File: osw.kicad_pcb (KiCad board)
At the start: 4 copper layers, 45.6 x 41.4 mm, 59 parts, among them J1 Conn_01x02, J2 microSD_MEM2067-02-180-00-A_R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, J3 2169890001, Q1 Q_NMOS_ToshibaSMD, SW1 SPST_EVQ-P7J01P, SW2 SPST_EVQ-P7J01P, SW3 SPST_EVQ-P7J01P, SW4 SPST_EVQ-P7J01P, U1 L96-M33, U10 BMA400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

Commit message: working on the layout.
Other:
- rule pad_to_mask_clearance: 0.051 -> 0
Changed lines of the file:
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@@
   (title_block
     (title "Open-Smartwatch-GPS")
-    (date "2022-12-16")
+    (date "2023-10-21")
     (rev "${REVISION}")
   )
   (layers
-    (0 "F.Cu" power)
+    (0 "F.Cu" signal)
     (1 "In1.Cu" signal)
     (2 "In2.Cu" signal)
@@
       (dielectric_constraints no)
     )
-    (pad_to_mask_clearance 0.051)
+    (pad_to_mask_clearance 0)
+    (aux_axis_origin 160 130.6)
+    (grid_origin 160 130.6)
     (pcbplotparams
       (layerselection 0x00010fc_ffffffff)
@@
   (gr_line (start 182.6 93.8) (end 182.6 124.5)
     (stroke (width 0.05) (type solid)) (layer "Edge.Cuts"))
-  (dimension (type orthogonal) (layer "F.Cu")
-    (pts (xy 164.975 89.625) (xy 175 89.2))
-    (height -4.425)
-    (orientation 0)
-    (gr_text "10.0250 mm" (at 169.9875 83.4) (layer "F.Cu")
-      (effects (font (size 1.5 1.5) (thickness 0.3)))
-    )
-    (format (prefix "") (suffix "") (units 3) (units_format 1) (precision 4))
-    (style (thickness 0.2) (arrow_length 1.27) (text_position_mode 0) (extension_height 0.58642) (extension_offset 0.5) keep_text_aligned)
-  )
-  (dimension (type orthogonal) (layer "F.Cu")
-    (pts (xy 155.225 89.625) (xy 145.2 89.8))
-    (height -4.425)
-    (orientation 0)
-    (gr_text "10.0250 mm" (at 150.2125 83.4) (layer "F.Cu")
-      (effects (font (size 1.5 1.5) (thickness 0.3)))
-    )
-    (format (prefix "") (suffix "") (units 3) (units_format 1) (precision 4))
-    (style (thickness 0.2) (arrow_length 1.27) (text_position_mode 0) (extension_height 0.58642) (extension_offset 0.5) keep_text_aligned)
-  )
   (zone (net 1) (net_name "GND") (layer "B.Cu") (hatch edge 0.508)
     (connect_pads (clearance 0.127))

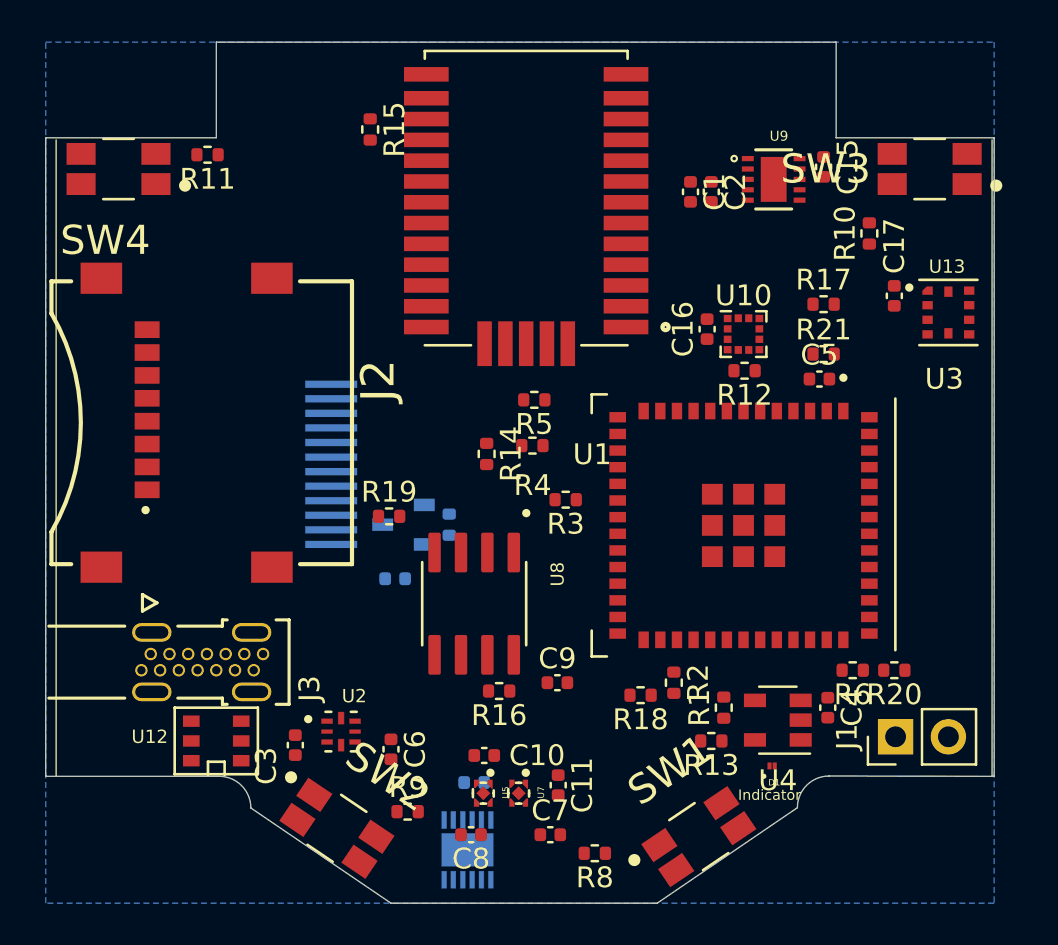
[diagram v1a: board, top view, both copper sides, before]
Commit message: Added some dimensions to the layout and corrected all the edge cuts so the board is symetric.
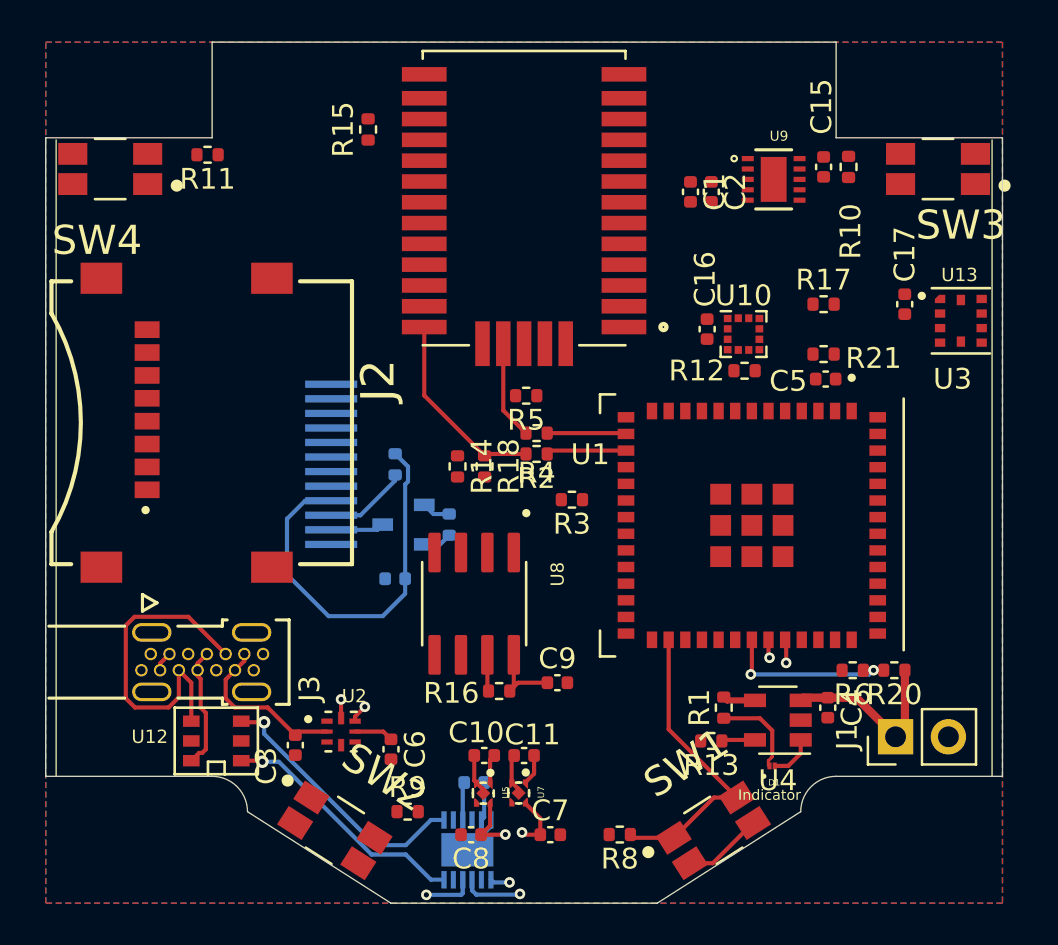
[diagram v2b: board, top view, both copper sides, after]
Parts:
- R19: moved to B.Cu
- moved R18 13.3 mm to (158.1, 109.6), turned to -90 degrees
- moved R2 12.8 mm to (160.6, 109.0), turned to 180 degrees
- moved R10 3.35 mm to (175.6, 95.2), turned to -90 degrees
- moved R19 2.52 mm to (153.8, 109.5), turned to -90 degrees
- moved C11 2.17 mm to (160.0, 123.5), turned to 180 degrees
- moved R14 1.52 mm to (156.8, 109.6)
- moved R8 1.50 mm to (164.6, 127.3)
- moved SW1 0.76 mm to (169.1, 127.1), turned to 32.52 degrees
- moved U13 0.72 mm to (181.0, 102.6)
- moved C17 0.64 mm to (178.3, 101.8)
- moved R4 0.63 mm to (160.6, 108.0)
- moved R5 0.44 mm to (160.1, 106.2)
- moved SW3 0.40 mm to (179.9, 95.3)
- moved SW4 0.40 mm to (140.1, 95.3)
- moved U3 0.40 mm to (170.9, 112.4)
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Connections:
- D1 pad 2: Net-(D1-A) -> /STAT_PWR
- R1 pad 1: Net-(D1-A) -> /STAT_PWR
- U3 pad 11: /SCL -> /TFT_CS
- U3 pad 12: /~{TFT_RST} -> /SCL
- U3 pad 13: /STAT_PWR -> /SDA
- U3 pad 14: unconnected-(U3-IO26-Pad14) -> /~{TFT_RST}
- U3 pad 15: /SDA -> /GPS_FON3V3
- U3 pad 16: /VLoad_EN -> /GPS_RX3V3
- U3 pad 21: /FLASH -> /RAM_HOLD
- U3 pad 23: GND -> unconnected-(U3-NC-Pad23)
- U3 pad 24: GND -> unconnected-(U3-NC-Pad24)
- U3 pad 28: GND -> unconnected-(U3-NC-Pad28)
- U3 pad 29: /TFT_CS -> /BTN2
- U3 pad 30: /GPS_RX3V3 -> /VLoad_EN
- U3 pad 31: /RAM_HOLD -> /STAT_PWR
- U3 pad 34: /BTN2 -> /B_MON
- U3 pad 37: GND -> unconnected-(U3-NC-Pad37)
- U3 pad 4: /B_MON -> unconnected-(U3-I36-Pad4)
- U3 pad 5: /3DFIX_3V3 -> /GEO_F3V3
- U3 pad 6: /GPS_FON3V3 -> /FLASH
- U3 pad 7: /GEO_F3V3 -> /3DFIX_3V3
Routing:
- net /TX: track 0.00 -> 26.2 mm, vias 0 -> 2
- net /3V3_2: track 0.00 -> 20.6 mm
- net /RX: track 0.00 -> 19.2 mm, vias 0 -> 2
- net /D_ESD-: track 0.00 -> 16.1 mm
- net /BTN2: track 0.00 -> 14.9 mm
- net /VCC: track 0.00 -> 14.3 mm, vias 0 -> 2
- net /VCC_SW: track 0.00 -> 13.7 mm, vias 0 -> 2
- net /D-: track 0.00 -> 13.0 mm, vias 0 -> 1
- net /D+: track 0.00 -> 12.1 mm, vias 0 -> 1
- net GND: track 0.00 -> 10.8 mm
- net /VBUS: track 0.00 -> 10.7 mm
- net /GPS_RX2V8: track 0.00 -> 9.42 mm
- net +3V3: track 0.00 -> 9.02 mm
- net /VBAT: track 0.00 -> 8.78 mm
- net /B_MON: track 0.00 -> 8.65 mm, vias 0 -> 2
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- added copper zone on F.Cu, net GND
- added copper zone on In1.Cu, net GND
- added copper zone on In2.Cu, net GND
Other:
- board size 45.6 x 41.4 mm -> 46 x 41.4 mm

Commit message: Updates to several footprints as they were not quite correct.  Finished layout.  All done on a simple two layer board.  Need to look over the design once more before ordering prototypes.
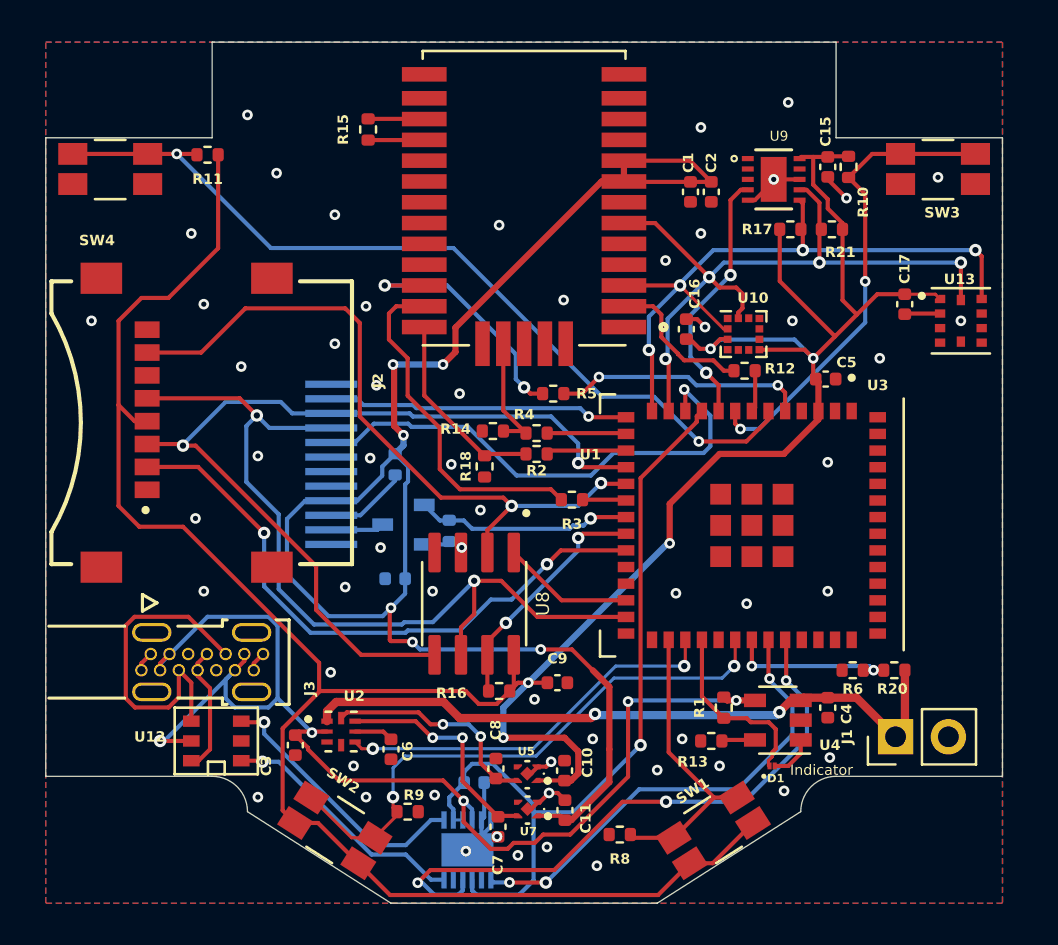
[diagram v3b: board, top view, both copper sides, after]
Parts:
- moved R21 6.01 mm to (174.8, 98.2), turned to 180 degrees
- moved R17 3.94 mm to (172.8, 98.2)
- moved C10 3.93 mm to (161.9, 124.2), turned to 90 degrees
- moved C8 3.40 mm to (158.6, 124.1), turned to 90 degrees
- moved C11 3.28 mm to (162.0, 126.1), turned to 90 degrees
- moved C7 2.54 mm to (158.7, 126.9), turned to -90 degrees
- moved R14 2.40 mm to (158.5, 107.9), turned to 180 degrees
- moved U5 2.31 mm to (160.2, 124.4), turned to 180 degrees
- moved R5 1.30 mm to (161.4, 106.1)
- moved C16 1.00 mm to (167.8, 103.0)
- moved U7 0.88 mm to (160.2, 126.1), turned to 180 degrees
- moved R7 0.30 mm to (156.4, 112.7)
- moved C15 0.20 mm to (174.6, 95.2)
- turned SW2 to -32.519 degrees
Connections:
- C16 pad 2: Net-(U10-GND) -> GND
- U10 pad 1: Net-(U10-GND) -> GND
- U10 pad 8: Net-(U10-GND) -> GND
- U10 pad 9: Net-(U10-GND) -> GND
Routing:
- net +3V3: track 9.02 -> 149.8 mm, vias 0 -> 5
- net /3V3_2: track 20.6 -> 75.3 mm, vias 0 -> 6
- net /VBUS: track 10.7 -> 59.2 mm, vias 0 -> 5
- net /MOSI: track 0.00 -> 43.3 mm, vias 0 -> 2
- net /SCLK: track 0.00 -> 41.5 mm, vias 0 -> 2
- net /FLASH: track 0.00 -> 41.0 mm, vias 0 -> 2
- net /SCL: track 0.00 -> 34.0 mm, vias 0 -> 4
- net /v3p3USB: track 4.74 -> 38.7 mm
- net /MISO: track 0.00 -> 33.7 mm, vias 0 -> 2
- net /SDA: track 0.00 -> 32.5 mm, vias 0 -> 4
- net /SD_CS: track 0.00 -> 29.5 mm, vias 0 -> 2
- net /BTN3: track 0.00 -> 27.4 mm, vias 0 -> 2
- net /TFT_CS: track 0.00 -> 24.5 mm, vias 0 -> 1
- net /VBAT: track 8.78 -> 32.9 mm, vias 0 -> 2
- net /EN: track 0.00 -> 23.0 mm, vias 0 -> 2
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- removed copper zone on In1.Cu, net GND
- removed copper zone on In2.Cu, net GND
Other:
- copper layers 4 -> 2

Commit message: Optimizing the layout a bit.
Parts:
- moved R3 0.90 mm to (161.4, 111.2)
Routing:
- net /SCLK: track 41.5 -> 37.0 mm
- net /3V3_2: track 75.3 -> 72.7 mm
- net /RAM_HOLD: track 11.6 -> 13.8 mm
- net +3V3: track 149.8 -> 147.6 mm
- net /SD_CS: track 29.5 -> 27.9 mm
- net /VCC_SW: track 11.1 -> 9.70 mm, vias 2 -> 0
- net /GPS_TX2V8: track 16.8 -> 15.9 mm
- net /GPS_TX3V3: track 2.11 -> 3.01 mm
- net /v3p3USB: track 38.7 -> 39.5 mm
- net /VCC: track 10.7 -> 9.91 mm, vias 2 -> 0
- net /RAM_CS: track 6.35 -> 7.03 mm
- net /GPS_FON2V8: track 5.87 -> 5.33 mm
- net GND: vias 57 -> 59

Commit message: Adding some silkscreen dressup.
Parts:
- added G1: LOGO, AllardFootPrints:aiLogo, B.Cu at (142.6, 100.4)
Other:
- board text added: "OSW Rev: ${REVISION} Eph 5:15-16"

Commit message: Finishing up the board.  Provided nothing jumps out looking through the DOCs later this should be good to order
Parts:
- moved R19 0.50 mm to (153.8, 110.0)
- moved Q1 0.44 mm to (154.6, 112.6)
- moved R7 0.41 mm to (156.8, 112.8)
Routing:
- net GND: track 21.3 -> 23.6 mm, vias 59 -> 63
- net /MOSI: track 42.8 -> 41.1 mm
- net /RAM_HOLD: track 13.8 -> 13.1 mm
- net /v3p3USB: track 39.5 -> 40.2 mm
- net /SCLK: track 37.0 -> 36.4 mm
